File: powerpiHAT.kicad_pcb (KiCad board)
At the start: 2 copper layers, 65 x 30 mm, 36 parts, among them J1 Conn_01x10, J2 AudioJack2_Dual_Ground_Switche, J3 40HAT, J4 AudioJack2_Dual_Ground_Switche, J5 AudioJack2_Dual_Ground_Switche, J6 AudioJack2_Dual_Ground_Switche, J9 CONN_01X02, Q1 DMG2305UX, Q2 DMMT5401, U2 CAT24C32

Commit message: Essentially, release 1.0.0 of the PowerPiHAT... we'll see if there's electrical changes necessary once we get a couple boards etched and populated.
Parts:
- removed J9: CONN_01X02, Connector_PinHeader_2.54mm:PinHeader_1x02_P2.54mm_Vertical
- removed R11: DNP, Resistor_SMD:R_0805_2012Metric_Pad1.15x1.40mm_HandSolder
- added H5: 3mm_Mounting_Hole, MountingHole:MountingHole_3.2mm_M3_DIN965, F.Cu at (112.7, 88.0)
- added H6: 3mm_Mounting_Hole, MountingHole:MountingHole_3.2mm_M3_DIN965, F.Cu at (133.0, 88.0)
- added J7: Barrel_Jack, project_footprints:BarrellJack-DC-902_SMT_Horizontal, F.Cu at (97.3, 70.3)
- C1, C4, R14, R2: moved to F.Cu
- U2: footprint Package_SOIC:SOIC-8_3.9x4.9mm_P1.27mm -> Package_SO:SOIC-8_3.9x4.9mm_P1.27mm
- moved H4 69.8 mm to (101.5, 113.0)
- moved C1 54.9 mm to (117.8, 99.6), turned to 180 degrees
- moved R2 51.7 mm to (121.6, 112.3), turned to 90 degrees
- moved R14 49.9 mm to (159.7, 76.7), turned to 180 degrees
- moved J2 49.6 mm to (117.8, 110.7)
- moved H3 48.4 mm to (159.5, 113.0)
- moved R10 45.2 mm to (158.4, 94.5), turned to 180 degrees
- moved R29 41.1 mm to (122.9, 69.1)
- moved C2 38.5 mm to (134.3, 99.6), turned to 180 degrees
- moved R8 37.8 mm to (116.5, 71.6), turned to 270 degrees
- moved R6 37.6 mm to (119.1, 71.6), turned to 270 degrees
- moved J1 36.8 mm to (111.5, 93.0), turned to 90 degrees
- moved U2 36.4 mm to (124.2, 74.2), turned to 90 degrees
- moved J6 36.3 mm to (157.2, 80.5), turned to 180 degrees
- moved C4 36.1 mm to (145.7, 85.6)
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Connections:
- J3 pad 1: (no net) -> /P3V3_HAT
- J3 pad 11: (no net) -> /WP_EEPROM
- R29 pad 1: /P3V3 -> /P3V3_HAT
- R29 pad 2: Net-(J9-Pad2) -> /WP_EEPROM
- R6 pad 1: /P3V3 -> /P3V3_HAT
- R8 pad 1: /P3V3 -> /P3V3_HAT
- U2 pad 7: Net-(J9-Pad2) -> /WP_EEPROM
- U2 pad 8: /P3V3 -> /P3V3_HAT
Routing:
- net /P5V_HAT: track 59.3 -> 144.0 mm, vias 1 -> 5
- net /ID_SC_EEPROM: track 24.1 -> 55.9 mm, vias 1 -> 3
- net /P3V3_HAT: track 0.00 -> 30.9 mm, vias 0 -> 2
- net /ADS_A1: track 61.1 -> 30.8 mm, vias 0 -> 1
- net /ADS_A0: track 58.1 -> 32.1 mm, vias 2 -> 1
- net /ID_SD_EEPROM: track 26.1 -> 48.9 mm
- net Net-(C3-Pad1): track 40.5 -> 17.8 mm
- net GND: track 249.3 -> 226.6 mm, vias 8 -> 3
- net Net-(J9-Pad2): track 22.6 -> 0.00 mm, vias 1 -> 0
- net Net-(C1-Pad1): track 42.7 -> 21.2 mm, vias 1 -> 0
- net Net-(C2-Pad1): track 42.3 -> 21.7 mm, vias 1 -> 0
- net Net-(C4-Pad1): track 34.4 -> 23.5 mm, vias 2 -> 0
- net /ADS_A3: track 43.0 -> 52.6 mm, vias 0 -> 1
- net /WP_EEPROM: track 0.00 -> 9.18 mm
- net /P3V3: track 7.31 -> 0.00 mm
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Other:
- board size 65 x 30 mm -> 65 x 56.5 mm
- board text added: "Pi Power Monitor HAT"
- board text added: "V 1.0.0 - Bryan Varner - 2019"

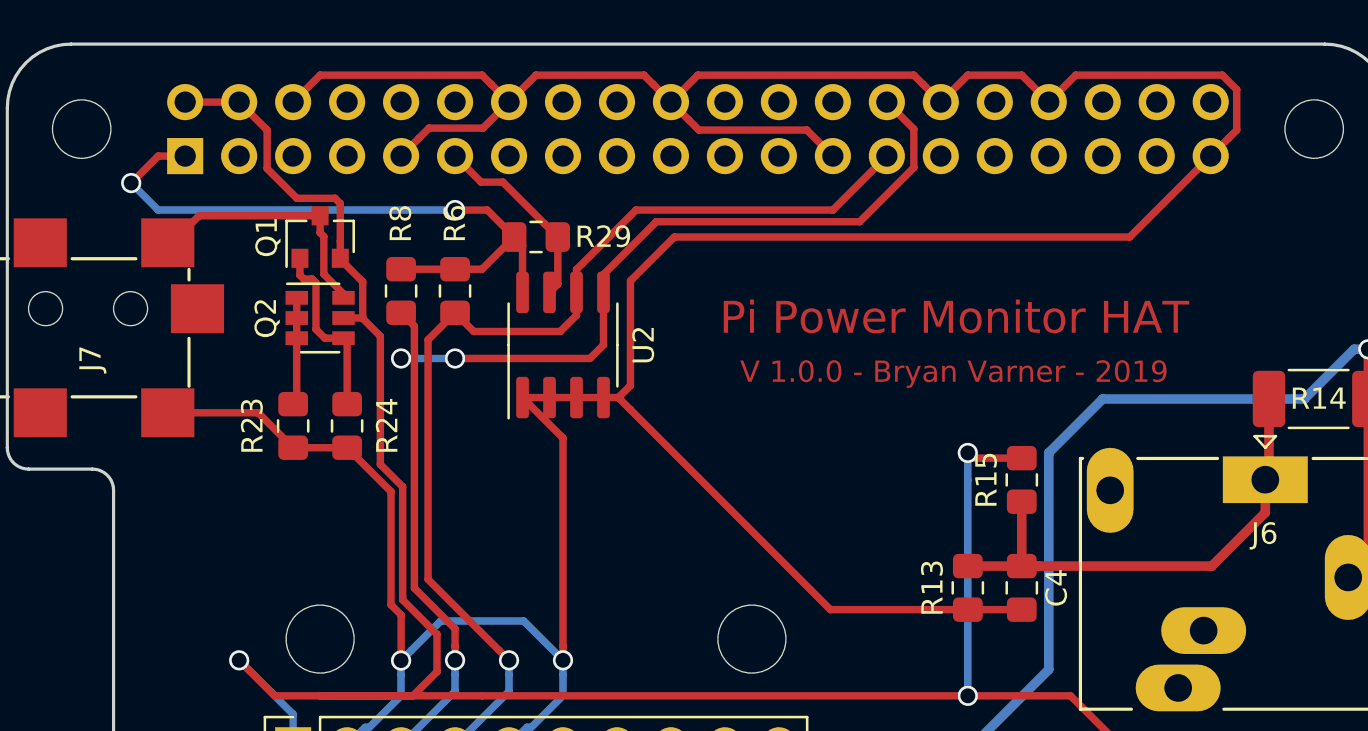
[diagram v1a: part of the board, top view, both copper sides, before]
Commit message: Include the UART on a breakout header, for additional bits later.
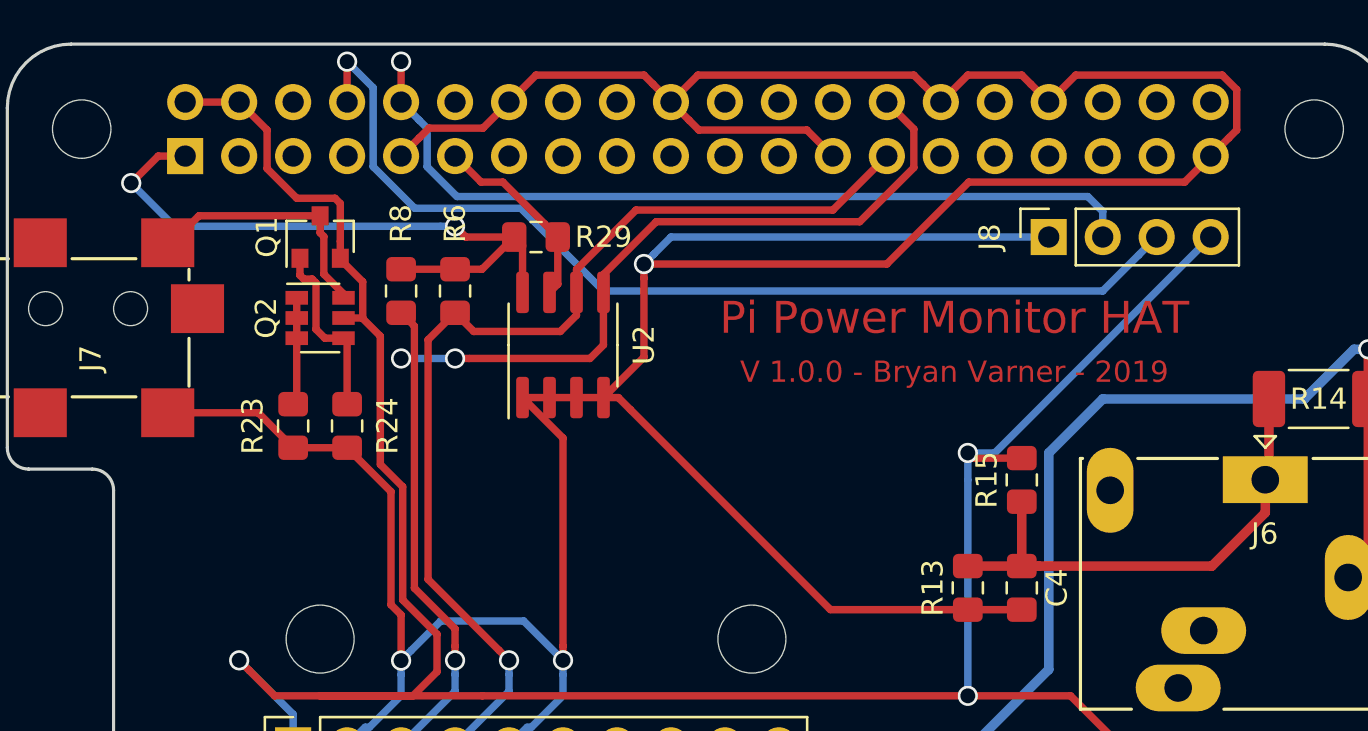
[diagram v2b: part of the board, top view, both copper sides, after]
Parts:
- added J8: Conn_01x04, Connector_PinSocket_2.54mm:PinSocket_1x04_P2.54mm_Vertical, F.Cu at (147.0, 69.1)
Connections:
- J3 pad 10: (no net) -> /PI_UART_RXD
- J3 pad 6: GND -> (no net)
- J3 pad 8: (no net) -> /PI_UART_TXD
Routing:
- net /PI_UART_TXD: track 0.00 -> 47.7 mm, vias 0 -> 1
- net /PI_UART_RXD: track 0.00 -> 39.3 mm, vias 0 -> 1
- net /P5V_HAT: track 144.0 -> 159.6 mm
- net GND: track 226.6 -> 235.4 mm, vias 3 -> 4

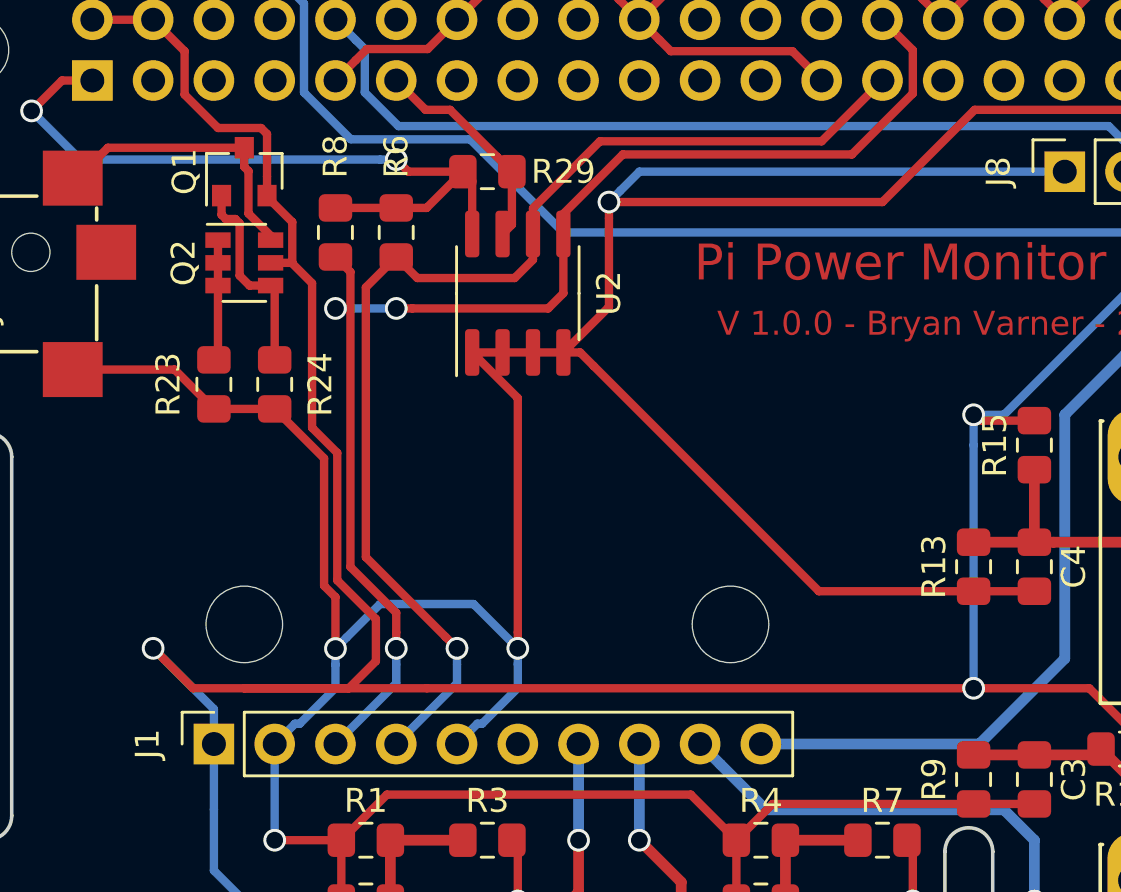
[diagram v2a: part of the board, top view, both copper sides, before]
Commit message: Breakout Header for 5v, Gnd, UART
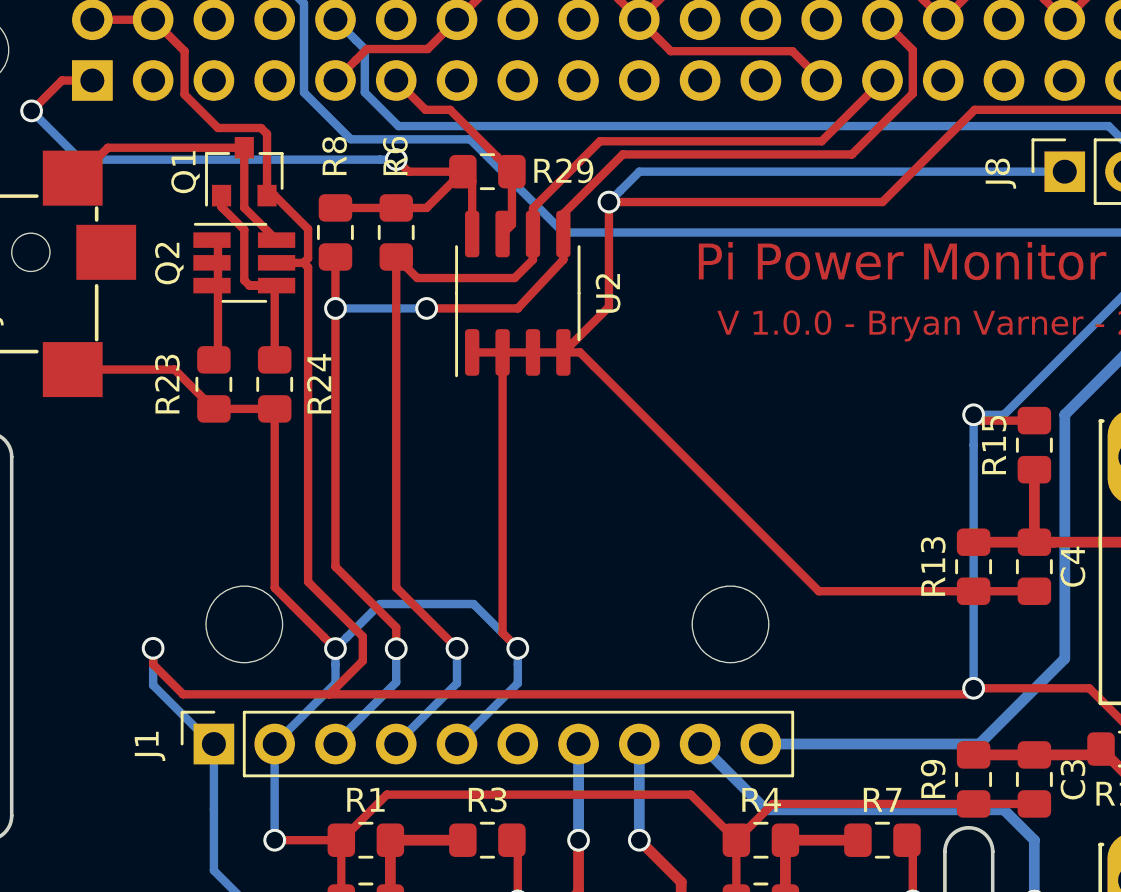
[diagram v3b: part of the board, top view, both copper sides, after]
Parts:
- Q2: footprint Package_TO_SOT_SMD:SOT-23-6 -> Package_TO_SOT_SMD:SOT-23-6_Handsoldering
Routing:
- net /P5V_HAT: track 159.6 -> 156.6 mm
- net /ID_SD_EEPROM: track 48.9 -> 47.8 mm
- net Net-(Q1-Pad1): track 8.53 -> 9.43 mm
- net /ID_SC_EEPROM: track 55.9 -> 55.1 mm
- net GND: track 235.4 -> 234.6 mm
